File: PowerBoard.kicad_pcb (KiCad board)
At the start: 2 copper layers, 212 parts, among them Q1 PSMN020-100YS, Q2 PSMN020-100YS, Q3 PSMN020-100YS, Q4 PSMN020-100YS, Q5 PSMN020-100YS, U1 LT8342RV-TRMPBF, U10 LM5050-1, U11 PINA745AIRELR, U12 TPS16851VMAR, U13 LM5050-1, U14 TPS16851VMAR, U15 LM5050-1, U16 TPS16851VMAR, U17 LM5050-1, U18 LMR43620MSC5RPERQ1, U2 AD5259BRMZ100, U3 ADAFRUIT_QT_PY, U4 TPS16851VMAR, U5 LM5050-1, U6 LT8342RV-TRMPBF, U7 PINA745AIRELR, U8 AD5259BRMZ100, U9 TPS16851VMAR

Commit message: Working on layout for dev board
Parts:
- removed C20, C25, C72, C77: 100pF, Capacitor_SMD:C_0603_1608Metric
- removed C21, C73: 10pF, Capacitor_SMD:C_0603_1608Metric
- removed C22, C74: 0.22uF, Capacitor_SMD:C_0603_1608Metric
- removed C23, C75: 4.7nF, Resistor_SMD:R_0603_1608Metric
- removed C24, C76: 22pF, Capacitor_SMD:C_0603_1608Metric
- removed C26, C78: 22nF, Capacitor_SMD:C_0805_2012Metric
- removed C27, C79: 100nF, Capacitor_SMD:C_0805_2012Metric
- removed C28, C43: 220pF, Capacitor_SMD:C_0603_1608Metric
- removed C29: 3.3nF, Capacitor_SMD:C_0603_1608Metric
- removed C30, C32, C34, C37, C38, C39, C42, C44, C45: 100nF, Capacitor_SMD:C_0603_1608Metric
- removed C31: 2.2uF, Capacitor_SMD:C_0603_1608Metric
- removed C33, C36, C40, C41, C46: 10uF, Capacitor_SMD:C_0805_2012Metric
- removed C35: 33uF, Capacitor_SMD:CP_Elec_6.3x5.8
- removed D1, D17, D18, D2: TPSMB28CA-VR, Diode_SMD:D_SMB
- removed D19, D20, D3, D4: BAT46GWJ, Diode_SMD:D_SOD-123
- removed FB3: FerriteBead, Capacitor_SMD:C_2220_5750Metric
- removed FB4: 74279252, Inductor_SMD:L_1812_4532Metric
- removed L2: 33uH, _Power_Board:IND_SER2918H-333KL
- removed Q1, Q5: PSMN020-100YS, Package_TO_SOT_SMD:LFPAK56
- removed R10, R65, R67, R8: 1Meg, Resistor_SMD:R_0603_1608Metric
- removed R11, R68: 67.3k, Resistor_SMD:R_0603_1608Metric
- removed R12, R69: 150, Resistor_SMD:R_0603_1608Metric
- removed R13, R70: 240k, Resistor_SMD:R_0603_1608Metric
- removed R14, R15, R71, R72: 33k, Resistor_SMD:R_0603_1608Metric
- removed R16, R73: 1.26k, Resistor_SMD:R_0603_1608Metric
- removed R17, R74: 464, Resistor_SMD:R_0603_1608Metric
- removed R18, R75: 1k, Resistor_SMD:R_0603_1608Metric
- removed R19, R76: 10, Resistor_SMD:R_1206_3216Metric
- removed R20, R77: 100, Resistor_SMD:R_0603_1608Metric
- removed R21, R23: 33.6k, Resistor_SMD:R_0603_1608Metric
- removed R22: 60.4k, Resistor_SMD:R_0603_1608Metric
- removed R24: 15k, Resistor_SMD:R_0603_1608Metric
- removed R25: 274k, Resistor_SMD:R_0603_1608Metric
- removed R66, R9: 36k, Resistor_SMD:R_0603_1608Metric
- removed U16, U4: TPS16851VMAR, _Power_Board:05-08-7040_ADI
- removed U17, U5: LM5050-1, Package_TO_SOT_SMD:TSOT-23-6
- removed U6: LT8342RV-TRMPBF, _Power_Board:05-08-7040_ADI
- removed U7: PINA745AIRELR, _Power_Board:REL0014A_PINA745AIRELR_TEX
- removed U8: AD5259BRMZ100, _Power_Board:RM_10_ADI
- R1: value 33.6k -> 31.6k
- U12, U14, U9: footprint _Power_Board:05-08-7040_ADI -> _Power_Board:VMA0023A-MFG
- moved C17 154.8 mm to (33.0, 169.2)
- moved C18 154.8 mm to (37.2, 174.1)
- moved R5 154.8 mm to (33.0, 174.2)
- moved R4 154.8 mm to (33.0, 171.7)
- moved U2 154.8 mm to (38.7, 170.3)
- moved Q2 144.8 mm to (218.6, 30.6)
- moved U12 140.8 mm to (35.5, 162.5)
- moved U10 137.5 mm to (225.6, 36.3)
- moved D11 136.8 mm to (45.9, 160.8)
- moved D12 136.8 mm to (45.9, 164.2)
- moved C62 132.9 mm to (53.6, 154.2)
- moved C63 132.9 mm to (53.6, 157.2)
- moved D10 131.0 mm to (47.2, 156.4)
- moved D9 131.0 mm to (47.2, 150.8)
- moved R50 128.9 mm to (51.6, 160.8)
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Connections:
- U3 pad 10: unconnected-(U3-A9/D9/MISO-Pad10) -> /Main/BOOSTY.EN
- U3 pad 7: unconnected-(U3-A6/D6/TX-Pad7) -> /Main/SX_B.EN
- U3 pad 8: unconnected-(U3-A7/D7/RX-Pad8) -> /Main/SY_B.EN
- U3 pad 9: unconnected-(U3-A8/D8/SCK-Pad9) -> /Main/BOOSTX.EN
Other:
- board outline added: 100 x 100 mm
- copper layers 2 -> 4

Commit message: Working layout
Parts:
- added NT10: NetTie_2, NetTie:NetTie-2_SMD_Pad0.5mm, F.Cu at (154.6, 84.7)
- added NT11: NetTie_2, NetTie:NetTie-2_SMD_Pad0.5mm, F.Cu at (152.3, 82.7)
- added NT12: NetTie_2, NetTie:NetTie-2_SMD_Pad0.5mm, F.Cu at (151.7, 80.8)
- added NT4: NetTie_2, NetTie:NetTie-2_SMD_Pad0.5mm, F.Cu at (155.0, 54.5)
- added NT5: NetTie_2, NetTie:NetTie-2_SMD_Pad0.5mm, F.Cu at (157.0, 52.2)
- added NT6: NetTie_2, NetTie:NetTie-2_SMD_Pad0.5mm, F.Cu at (158.9, 51.6)
- added NT7: NetTie_2, NetTie:NetTie-2_SMD_Pad0.5mm, F.Cu at (178.3, 84.7)
- added NT8: NetTie_2, NetTie:NetTie-2_SMD_Pad0.5mm, F.Cu at (176.0, 82.7)
- added NT9: NetTie_2, NetTie:NetTie-2_SMD_Pad0.5mm, F.Cu at (175.4, 80.8)
- C54, C63, C71: footprint Capacitor_SMD:C_0805_2012Metric -> Capacitor_SMD:C_0603_1608Metric
- Q2, Q3, Q4: footprint Package_TO_SOT_SMD:LFPAK56 -> _Power_Board:LFPAK56_1
- moved C61 170.4 mm to (190.2, 89.5), turned to 90 degrees
- moved D12 167.4 mm to (188.6, 76.6)
- moved R44 165.9 mm to (189.4, 87.0)
- moved C60 164.9 mm to (186.8, 93.2), turned to -90 degrees
- moved D11 162.1 mm to (188.6, 83.8)
- moved U12 162.1 mm to (181.1, 91.3), turned to 180 degrees
- moved D10 160.8 mm to (188.8, 80.2), turned to 180 degrees
- moved R49 158.6 mm to (188.6, 89.5), turned to 90 degrees
- moved R47 157.2 mm to (190.2, 93.2), turned to -90 degrees
- moved R48 156.5 mm to (188.6, 93.2), turned to -90 degrees
- moved R39 156.2 mm to (175.4, 93.4)
- moved C59 154.5 mm to (175.4, 90.2), turned to 180 degrees
- moved C58 154.2 mm to (175.4, 88.6), turned to 180 degrees
- moved R43 152.1 mm to (175.4, 87.0), turned to 180 degrees
- moved R46 151.9 mm to (172.2, 88.6), turned to 180 degrees
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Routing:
- net VBUS: track 0.00 -> 23.6 mm
- net +5V: track 0.00 -> 14.9 mm, vias 0 -> 6
- net Net-(U9-OVP): track 0.00 -> 9.21 mm
- net Net-(U14-OVP): track 0.00 -> 9.21 mm
- net Net-(U12-OVP): track 0.00 -> 9.21 mm
- net Net-(U18-BOOT): track 0.00 -> 8.47 mm
- net Net-(U10-GATE): track 0.00 -> 8.41 mm
- net Net-(U13-GATE): track 0.00 -> 8.41 mm
- net Net-(U15-GATE): track 0.00 -> 8.41 mm
- net Net-(Q2-PadG): track 0.00 -> 8.19 mm
- net Net-(Q3-PadG): track 0.00 -> 8.19 mm
- net Net-(Q4-PadG): track 0.00 -> 8.19 mm
- net Net-(U2-A): track 0.00 -> 7.27 mm
- net Net-(U14-IREF): track 0.00 -> 6.78 mm
- net Net-(U9-IREF): track 0.00 -> 6.78 mm
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- added copper zone on F.Cu, net +5V
- added copper zone on In2.Cu, net +5V
- added copper zone on F.Cu, net /Main/batt1_load_sw/IN
- added copper zone on F.Cu, net /Main/batt2_load_sw/IN
- added copper zone on F.Cu, net /Main/boost_a_frontend/BOOST_OUT
- added copper zone on F.Cu, net /Main/boost_a_frontend/PANEL_IN
- added copper zone on F.Cu, net /Main/boost_a_frontend/Vout
- added copper zone on F.Cu, net GND
- added copper zone on F.Cu, net Net-(C10-Pad1)
- added copper zone on F.Cu, net Net-(D10-A2)
- added copper zone on F.Cu, net Net-(D14-A2)
- added copper zone on F.Cu, net Net-(D6-A2)
- added copper zone on F.Cu, net Net-(U1-VIN)
- added copper zone on F.Cu, net VBUS

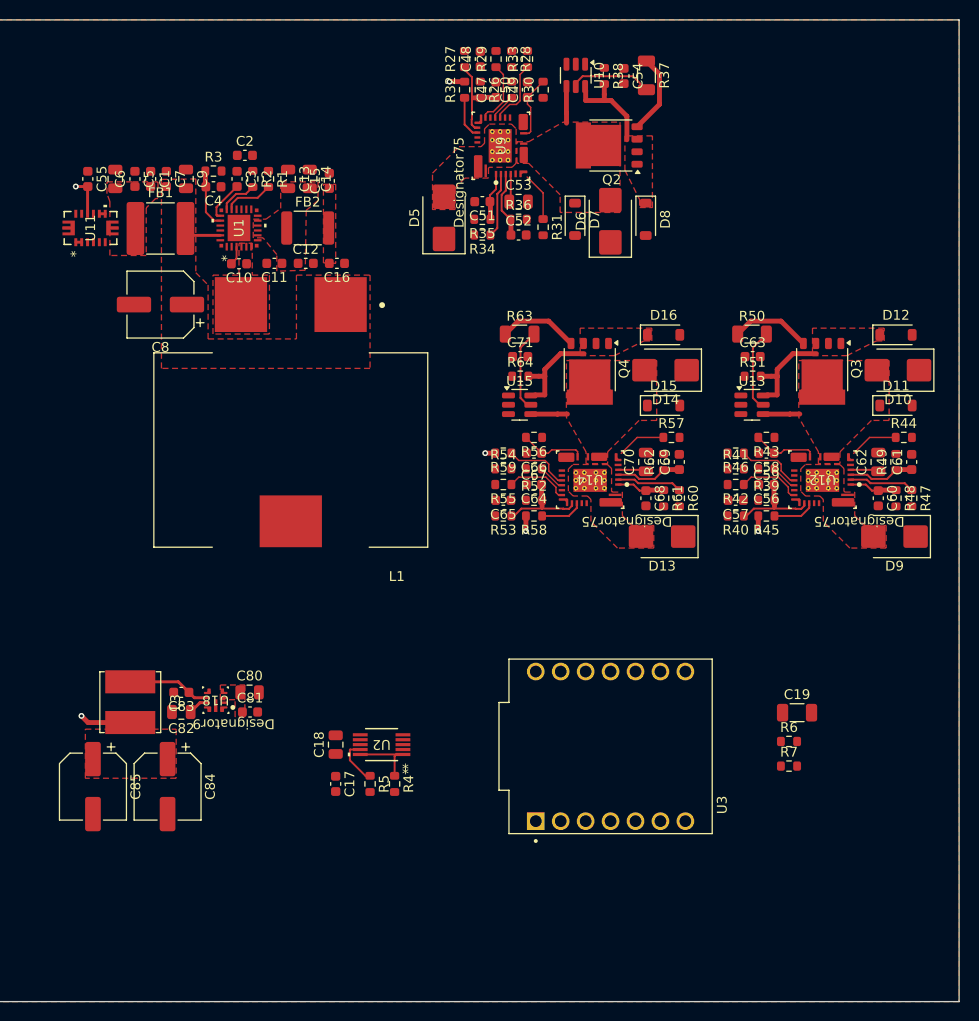
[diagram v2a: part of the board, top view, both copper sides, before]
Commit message: Working on layout. Adding in TPs to schematic
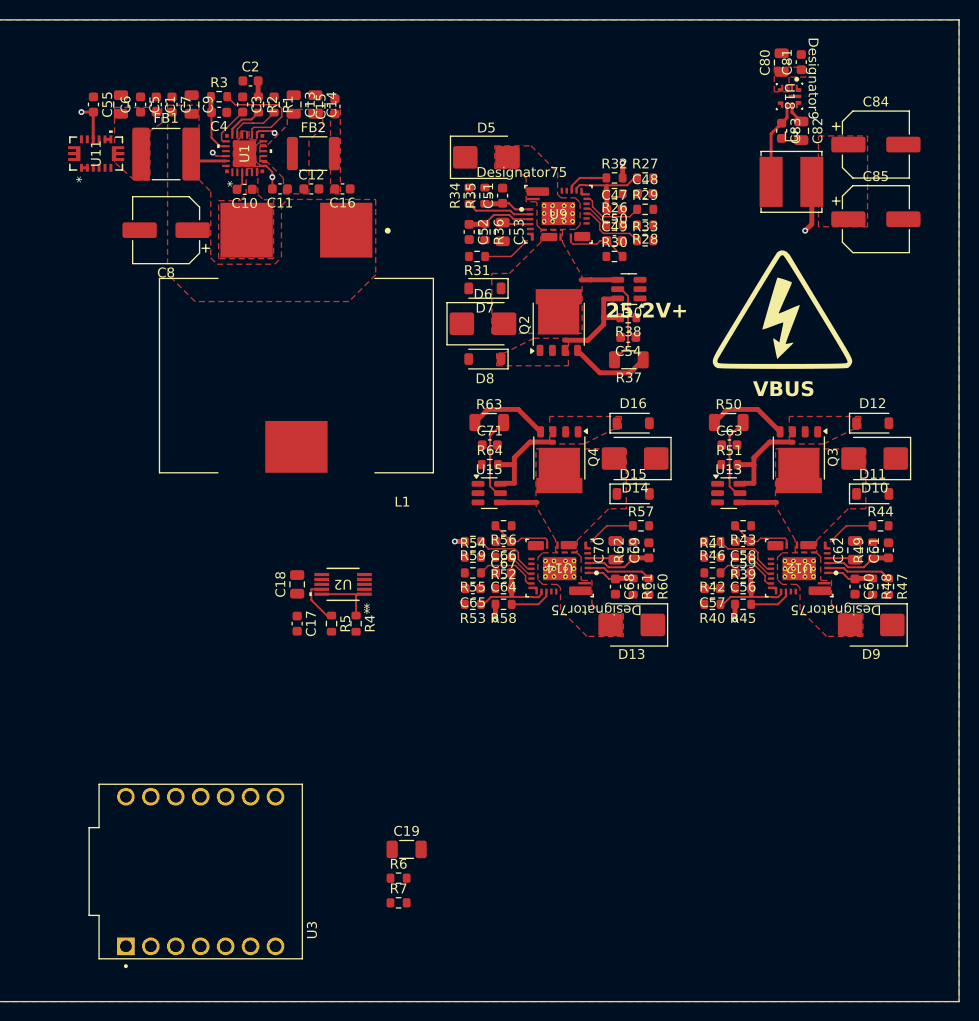
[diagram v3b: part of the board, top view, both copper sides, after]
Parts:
- added G***: LOGO, LOGO, F.Cu at (177.0, 74.0)
- moved C85 98.5 mm to (186.5, 64.8), turned to 0 degrees
- moved C84 97.4 mm to (186.5, 57.2), turned to 0 degrees
- moved C81 86.8 mm to (178.9, 48.8), turned to 90 degrees
- moved C82 86.6 mm to (178.9, 55.8), turned to -90 degrees
- moved L3 85.7 mm to (177.9, 61.0), turned to 0 degrees
- moved U18 84.8 mm to (177.7, 52.3), turned to -90 degrees
- moved C80 84.0 mm to (176.9, 48.9), turned to 90 degrees
- moved C83 83.7 mm to (176.9, 55.8), turned to -90 degrees
- moved U3 43.7 mm to (117.8, 131.2)
- moved C19 42.1 mm to (138.7, 129.0)
- moved R6 42.1 mm to (137.9, 131.9)
- moved R7 42.1 mm to (137.9, 134.4)
- moved R37 29.0 mm to (161.4, 79.1), turned to 180 degrees
- moved C54 26.6 mm to (161.3, 76.8), turned to 180 degrees
- moved R38 24.7 mm to (161.3, 74.8), turned to 180 degrees
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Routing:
- net Net-(U1-VSET1): track 0.00 -> 11.0 mm
- net GND: track 0.00 -> 2.89 mm, vias 0 -> 1
- net /Main/SX_B.FB: track 0.00 -> 2.16 mm, vias 0 -> 1
- net Net-(C2-Pad2): track 0.00 -> 1.59 mm
- net /Main/SX_B.EN: track 0.00 -> 1.49 mm, vias 0 -> 1
- added copper zone on In1.Cu, net GND
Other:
- board text added: "25.2V+"
- board text added: "VBUS"

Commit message: Working on layout still
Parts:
- G***: value LOGO -> VBUS
- moved R4 51.5 mm to (102.8, 64.7), turned to 0 degrees
- moved U2 49.1 mm to (98.8, 66.0), turned to -90 degrees
- moved R5 48.0 mm to (102.8, 67.2), turned to 0 degrees
- moved C17 43.1 mm to (102.8, 70.7), turned to 0 degrees
- moved C18 42.5 mm to (98.8, 70.7), turned to 180 degrees
- moved C19 28.2 mm to (111.4, 135.8), turned to 180 degrees
- moved C80 19.0 mm to (167.3, 65.3), turned to 180 degrees
- moved C81 18.6 mm to (167.3, 63.3), turned to 180 degrees
- moved U18 14.0 mm to (170.8, 64.5), turned to 0 degrees
- moved R7 11.9 mm to (134.7, 123.0)
- moved C84 10.9 mm to (175.7, 55.7), turned to 90 degrees
- moved C83 9.86 mm to (174.3, 65.3), turned to 0 degrees
- moved C85 9.65 mm to (183.3, 55.7), turned to 90 degrees
- moved C82 8.81 mm to (174.3, 63.3), turned to 0 degrees
- moved R6 6.99 mm to (134.7, 125.7), turned to 180 degrees
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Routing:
- net +5V: track 14.9 -> 27.4 mm, vias 6 -> 17
- net Net-(D10-A2): track 0.00 -> 5.67 mm
- net Net-(U12-SFT_SEL): track 4.96 -> 0.00 mm
- net /Main/SCL: track 0.00 -> 2.80 mm
- net /Main/SDA: track 0.00 -> 2.78 mm
- net GND: track 2.89 -> 3.60 mm
- added copper zone on B.Cu, net GND
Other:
- board text added: "BATT1"
- board text added: "BATT2"
- board text removed: "VBUS"

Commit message: Working on it
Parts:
- removed C19: 100nF, Capacitor_SMD:C_1206_3216Metric
- removed C47, C52, C56, C61, C64, C69: 100pF, Capacitor_SMD:C_0603_1608Metric
- removed C48, C57, C65: 10pF, Capacitor_SMD:C_0603_1608Metric
- removed C49, C58, C66: 0.22uF, Capacitor_SMD:C_0603_1608Metric
- removed C50, C59, C67: 4.7nF, Resistor_SMD:R_0603_1608Metric
- removed C51, C60, C68: 22pF, Capacitor_SMD:C_0603_1608Metric
- removed C53, C62, C70: 22nF, Capacitor_SMD:C_0805_2012Metric
- removed C54, C63, C71, C81, C83: 100nF, Capacitor_SMD:C_0603_1608Metric
- removed C80: 4.7uF, Capacitor_SMD:C_0805_2012Metric
- removed C82: 1uF, Capacitor_SMD:C_0805_2012Metric
- removed C84, C85: 22uF, Capacitor_SMD:CP_Elec_6.3x5.9
- removed D10, D13, D14, D5, D6, D9: TPSMB28CA-VR, Diode_SMD:D_SMB
- removed D11, D12, D15, D16, D7, D8: BAT46GWJ, Diode_SMD:D_SOD-123
- removed G***: VBUS, LOGO
- removed L3: 3.3uH, Inductor_SMD:L_Bourns_SRN6045TA
- removed NT10, NT11, NT12, NT4, NT5, NT6, NT7, NT8, NT9: NetTie_2, NetTie:NetTie-2_SMD_Pad0.5mm
- removed Q2, Q3, Q4: PSMN020-100YS, _Power_Board:LFPAK56_1
- removed R26, R28, R39, R41, R52, R54: 1Meg, Resistor_SMD:R_0603_1608Metric
- removed R27, R40, R53: 36k, Resistor_SMD:R_0603_1608Metric
- removed R29, R42, R55: 67.3k, Resistor_SMD:R_0603_1608Metric
- removed R30, R43, R56: 150, Resistor_SMD:R_0603_1608Metric
- removed R31, R44, R57: 240k, Resistor_SMD:R_0603_1608Metric
- removed R32, R33, R45, R46, R58, R59, R6, R7: 33k, Resistor_SMD:R_0603_1608Metric
- removed R34, R47, R60: 1.26k, Resistor_SMD:R_0603_1608Metric
- removed R35, R48, R61: 464, Resistor_SMD:R_0603_1608Metric
- removed R36, R49, R62: 1k, Resistor_SMD:R_0603_1608Metric
- removed R37, R50, R63: 10, Resistor_SMD:R_1206_3216Metric
- removed R38, R51, R64: 100, Resistor_SMD:R_0603_1608Metric
- removed U10, U13, U15: LM5050-1, Package_TO_SOT_SMD:TSOT-23-6
- removed U12, U14, U9: TPS16851VMAR, _Power_Board:VMA0023A-MFG
- removed U18: LMR43620MSC5RPERQ1, _Power_Board:RPE0009A-MFG
- removed U3: ADAFRUIT_QT_PY, _Power_Board:MODULE_ADAFRUIT_QT_PY
- L1: footprint _Power_Board:IND_SER2918H-333KL -> _PowerBoard:IND_SER2918H-333KL
- U1: footprint _Power_Board:05-08-7040_ADI -> _PowerBoard:05-08-7040_ADI
- U11: footprint _Power_Board:REL0014A_PINA745AIRELR_TEX -> _PowerBoard:REL0014A_PINA745AIRELR_TEX
- U2: footprint _Power_Board:RM_10_ADI -> _PowerBoard:RM_10_ADI
- moved C18 41.8 mm to (138.7, 58.0), turned to -90 degrees
- moved C17 39.6 mm to (138.7, 54.0), turned to 90 degrees
- moved U2 36.1 mm to (134.0, 58.0), turned to 0 degrees
- moved R5 35.0 mm to (135.2, 54.0), turned to 90 degrees
- moved R4 31.7 mm to (132.7, 54.0), turned to 90 degrees
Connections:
- C15 pad 1: /Main/boost_a_frontend/BOOST_OUT -> /Main/boost_a_control/VOUT_IN
- C16 pad 2: /Main/boost_a_frontend/BOOST_OUT -> /Main/boost_a_control/VOUT_IN
- FB2 pad 2: /Main/boost_a_frontend/BOOST_OUT -> /Main/boost_a_control/VOUT_IN
- R4 pad 1: Net-(U2-A) -> /Main/SX_B.FB
- R4 pad 2: /Main/SX_B.FB -> /Main/boost_a_control/VOUT_IN
- U2 pad 1: Net-(U2-A) -> /Main/SX_B.FB
- U2 pad 10: Net-(U2-A) -> /Main/SX_B.FB
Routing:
- net /Main/SDA: track 2.78 -> 32.2 mm, vias 0 -> 2
- net /Main/SCL: track 2.80 -> 29.7 mm, vias 0 -> 2
- net VBUS: track 23.6 -> 0.00 mm
- net /Main/SX_B.FB: track 2.16 -> 20.5 mm, vias 1 -> 0
- net +5V: track 27.4 -> 11.2 mm, vias 17 -> 2
- net Net-(U14-OVP): track 9.21 -> 0.00 mm
- net Net-(U12-OVP): track 9.21 -> 0.00 mm
- net Net-(U9-OVP): track 9.21 -> 0.00 mm
- net Net-(U18-BOOT): track 8.47 -> 0.00 mm
- net Net-(U15-GATE): track 8.41 -> 0.00 mm
- net Net-(U13-GATE): track 8.41 -> 0.00 mm
- net Net-(U10-GATE): track 8.41 -> 0.00 mm
- net Net-(Q2-PadG): track 8.19 -> 0.00 mm
- net Net-(Q4-PadG): track 8.19 -> 0.00 mm
- net Net-(Q3-PadG): track 8.19 -> 0.00 mm
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- added copper zone on F.Cu, net /Main/boost_a_control/VOUT_IN
- removed copper zone on F.Cu, net +5V
- removed copper zone on F.Cu, net /Main/batt1_load_sw/IN
- removed copper zone on F.Cu, net /Main/batt2_load_sw/IN
- removed copper zone on F.Cu, net /Main/boost_a_frontend/BOOST_OUT
- removed copper zone on F.Cu, net Net-(D10-A2)
- removed copper zone on F.Cu, net Net-(D14-A2)
- removed copper zone on F.Cu, net Net-(D6-A2)
- removed copper zone on F.Cu, net VBUS
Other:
- board text removed: "25.2V+"
- board text removed: "BATT1"
- board text removed: "BATT2"
